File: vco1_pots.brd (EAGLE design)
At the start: 106 x 50 mm, 30 parts

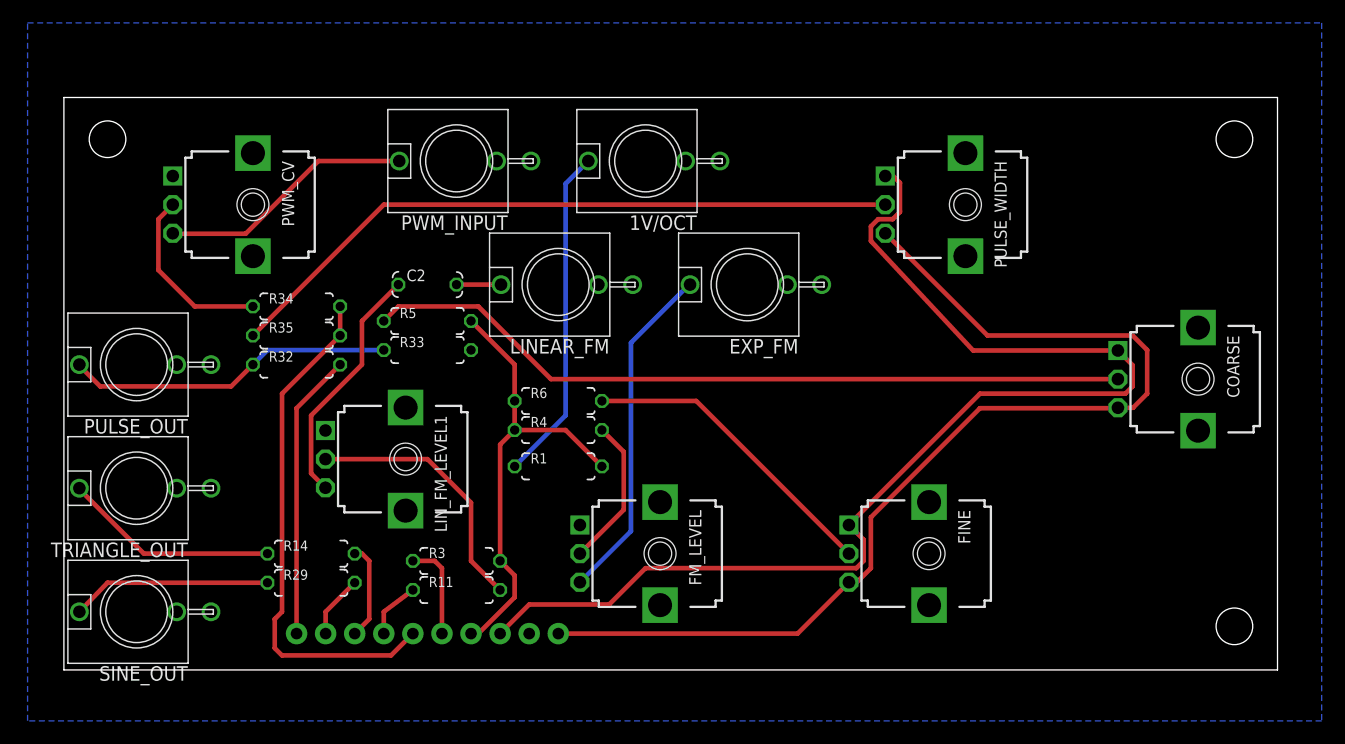
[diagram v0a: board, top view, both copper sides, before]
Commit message: Rename one of the R3s to R37
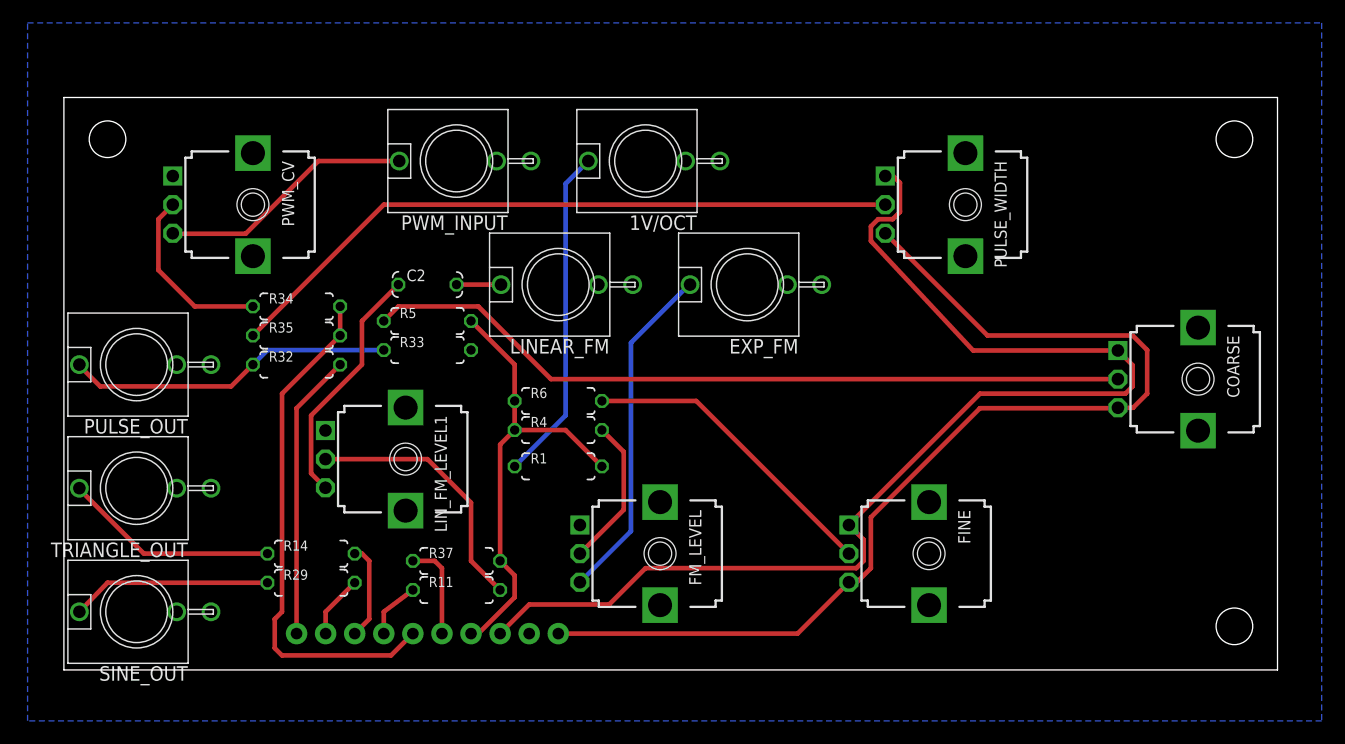
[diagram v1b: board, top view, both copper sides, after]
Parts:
- renumbered R3 to R37
